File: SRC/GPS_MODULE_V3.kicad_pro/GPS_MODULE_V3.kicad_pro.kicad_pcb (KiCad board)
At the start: 4 copper layers, 53.7 x 41 mm, 141 parts, among them J1 Input, J2 Conn_02x02_Odd_Even, J3 nano_sim, J5 Conn_02x03_Odd_Even, Q1 SSM3J328R-HXY, Q2 BSN20, Q3 BSN20, Q5 2N7002, Q6 2N7002, Q7 2N7002, Q8 2N7002, Q9 2N7002, U1 ADP2504ACPZ-R7_3.3V_VERSION, U2 STM32F103C8Tx, U3 SIM7000E, U4 MAX485E, U7 ATA6561-GAQW-N, U8 W25Q32JVSS, Y1 8MHz, Y2 32.678KHz

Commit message: added logo
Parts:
- added G***: LOGO, MACHADA_footprints:ECOBODDA_medium, F.Cu at (247.8, 69.3)
- added G***: LOGO, MACHADA_footprints:GEVITON_LOGO_small, B.Cu at (271.5, 76.8)
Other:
- board text added: "001211223"
- board text added: "MADE IN KENYA"

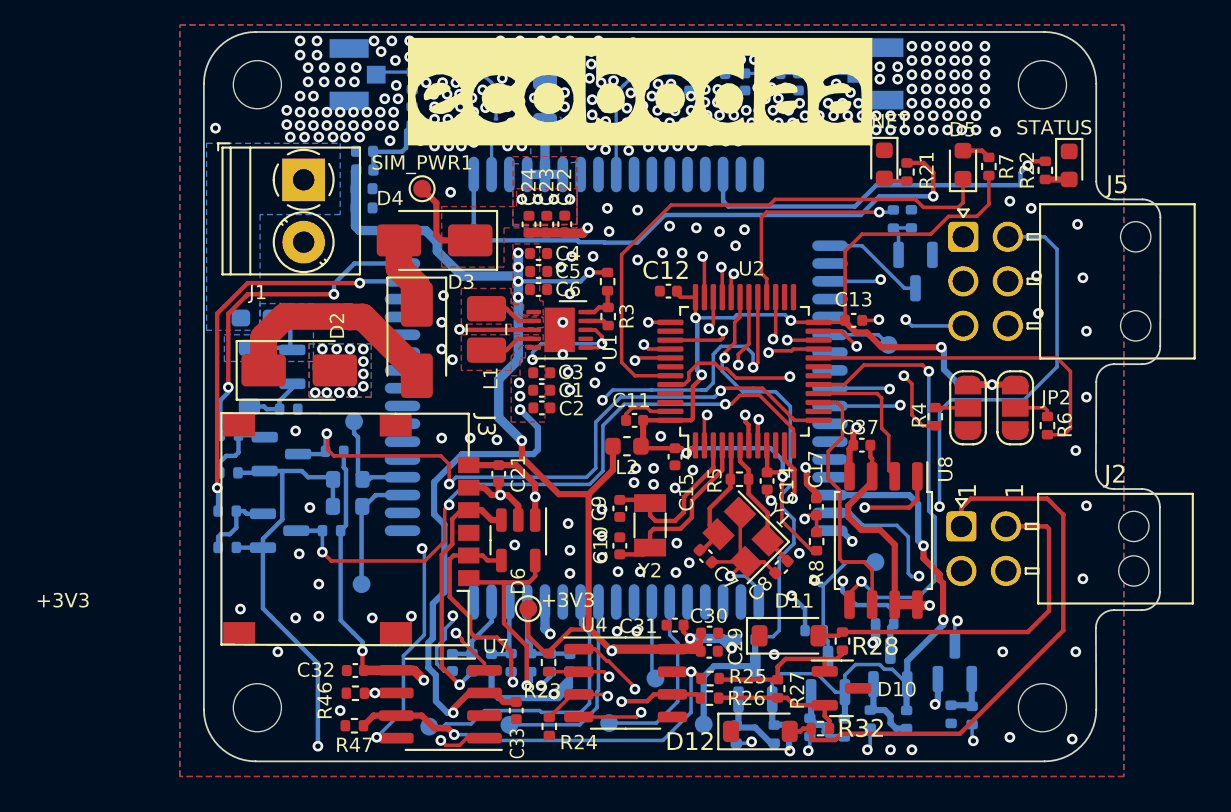
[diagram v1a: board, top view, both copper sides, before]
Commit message: gps update on buck 3v3
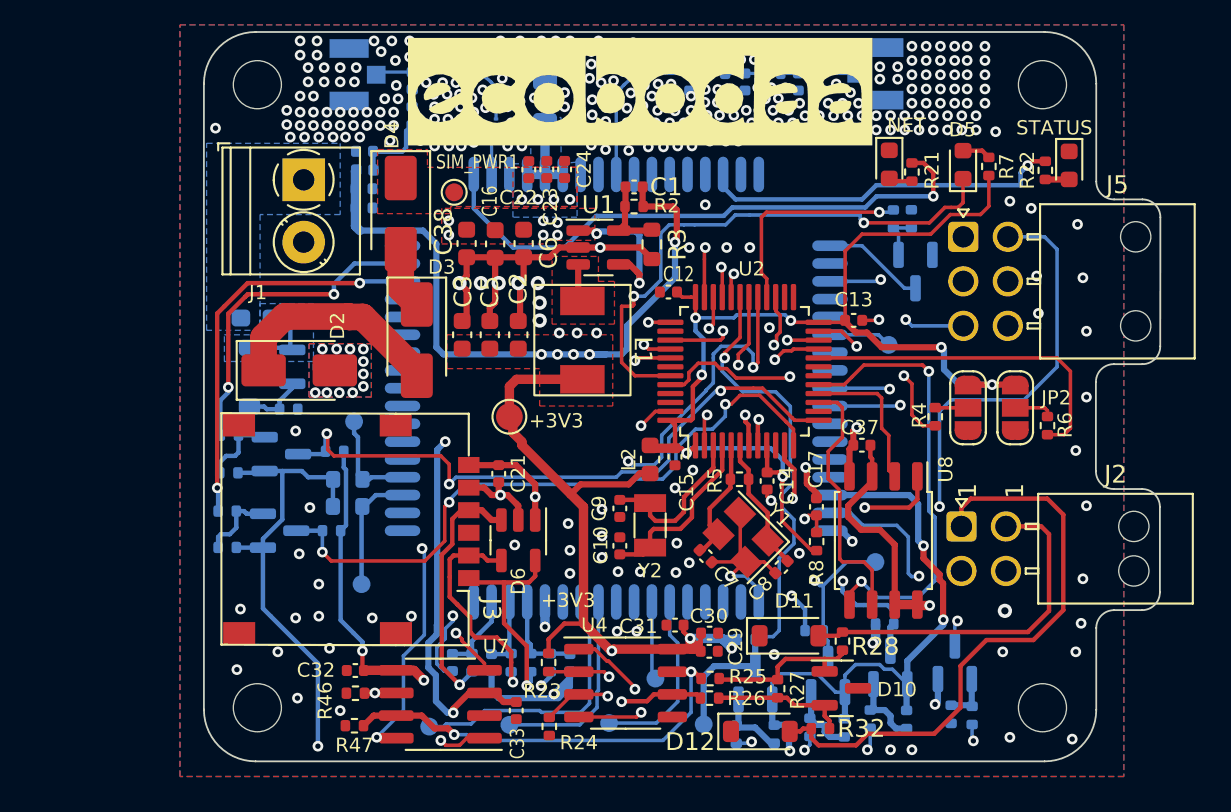
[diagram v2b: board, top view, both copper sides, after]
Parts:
- removed C11: 100n, Capacitor_SMD:C_0402_1005Metric
- removed C4: 10u, Capacitor_SMD:C_0402_1005Metric
- added C16: 10u, Capacitor_SMD:C_0603_1608Metric, F.Cu at (239.7, 77.9)
- added C38: 100n, Capacitor_SMD:C_0603_1608Metric, F.Cu at (238.1, 77.9)
- C1: value 10u -> 8.2p
- C2: value 100n -> 10n; footprint Capacitor_SMD:C_0402_1005Metric -> Capacitor_SMD:C_0603_1608Metric
- C3: value 10u -> 33p; footprint Capacitor_SMD:C_0402_1005Metric -> Capacitor_SMD:C_0603_1608Metric
- C5: value 100n -> 22u; footprint Capacitor_SMD:C_0402_1005Metric -> Capacitor_SMD:C_0603_1608Metric
- C6: footprint Capacitor_SMD:C_0402_1005Metric -> Capacitor_SMD:C_0603_1608Metric
- L1: value 1.5uH -> 2.2u; footprint Inductor_SMD:L_1008_2520Metric_Pad1.43x2.20mm_HandSolder -> greencharge-footprints:MDA5030-100M
- R2: value 1K -> 180K
- R3: value 1K -> 40K; footprint Resistor_SMD:R_0402_1005Metric -> Resistor_SMD:R_0603_1608Metric
- TP2: footprint TestPoint:TestPoint_Pad_D1.0mm -> TestPoint:TestPoint_Pad_D1.5mm
- U1: value ADP2504ACPZ-R7_3.3V_VERSION -> SY8089AAAC; footprint Package_DFN_QFN:DFN-10-1EP_3x3mm_P0.5mm_EP1.7x2.5mm -> Package_TO_SOT_SMD:SOT-23-5
- moved C1 12.5 mm to (247.5, 74.7), turned to 180 degrees
- moved TP2 10.8 mm to (240.5, 87.6)
- moved L1 5.62 mm to (244.6, 81.1), turned to -90 degrees
- moved U1 5.11 mm to (245.5, 78.1)
- moved C3 4.95 mm to (237.8, 83.0), turned to 90 degrees
- moved R3 4.74 mm to (248.5, 77.9)
- moved C5 4.49 mm to (239.4, 83.0), turned to 90 degrees
- moved R2 4.47 mm to (247.5, 75.8), turned to 180 degrees
- moved C2 4.31 mm to (241.0, 83.0), turned to 90 degrees
- moved C24 3.67 mm to (243.6, 73.7), turned to 90 degrees
- moved C22 3.67 mm to (241.6, 73.7), turned to 90 degrees
- moved C23 3.08 mm to (242.6, 73.7), turned to 90 degrees
- moved C6 2.71 mm to (241.3, 77.9), turned to -90 degrees
- moved D4 2.42 mm to (234.4, 76.2), turned to -90 degrees
- moved SIM_PWR1 1.81 mm to (237.4, 75.0)
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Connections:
- C1 pad 1: +5V -> +3V3
- C1 pad 2: GND -> Net-(U1-FB)
- C2 pad 1: +5V -> +3V3
- C3 pad 1: +5V -> +3V3
- C6 pad 1: +3V3 -> +5V
- L1 pad 1: Net-(U1-SW1) -> Net-(U1-LX)
- L1 pad 2: Net-(U1-SW2) -> +3V3
- U1 pad 1: +3V3 -> +5V
- U1 pad 2: Net-(U1-SW2) -> GND
- U1 pad 3: GND -> Net-(U1-LX)
- U1 pad 4: Net-(U1-SW1) -> +5V
- U1 pad 5: +5V -> Net-(U1-FB)
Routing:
- net GND: track 56.2 -> 69.3 mm, vias 396 -> 382
- net +3V3: track 131.5 -> 142.6 mm, vias 14 -> 13
- net 4.2V_SIMPWR: track 9.71 -> 4.75 mm
- net Net-(U1-SW2): track 2.93 -> 0.00 mm
- net Net-(U1-SW1): track 2.91 -> 0.00 mm
- net Net-(U1-FB): track 2.32 -> 4.49 mm
- net Net-(U1-LX): track 0.00 -> 2.15 mm
- net /STM32F103C8T6_MCU/3v3_stm: track 67.1 -> 65.2 mm
- net +5V: track 76.2 -> 78.1 mm, vias 17 -> 21
- net /CAN_TRANSCEIVER_ATA6561/CAN_RX: track 37.4 -> 38.8 mm
- net /CAN_TRANSCEIVER_ATA6561/CAN_TX: track 46.2 -> 47.4 mm
- net /RS485_MAX485/A: track 32.5 -> 33.3 mm
- net /SIM7000E_GPRS_SIM MODULE/STATUS: track 21.2 -> 20.4 mm
- net /STM32F103C8T6_MCU/RX2: track 37.1 -> 36.3 mm
- net /SIM7000E_GPRS_SIM MODULE/V_Sim: track 20.3 -> 19.5 mm
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- added copper zone on F.Cu, net Net-(U1-LX)
- removed copper zone on F.Cu, net Net-(U1-SW1)
- removed copper zone on F.Cu, net Net-(U1-SW2)

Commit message: updates on BOM, CPL and gerbers
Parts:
- removed BOOT_CFG1: BOOT_CFG, TestPoint:TestPoint_Pad_D1.0mm
- removed C35: 10n, Capacitor_SMD:C_0402_1005Metric
- removed C36: 1n, Capacitor_SMD:C_0402_1005Metric
- removed FL1: B39162B8813P810, Filter:Filter_1109-5_1.1x0.9mm
- removed the G*** at (247.8, 69.3)
- removed J5: Conn_02x03_Odd_Even, Connector_Molex:Molex_Nano-Fit_105314-xx06_2x03_P2.50mm_Horizontal
- removed L4: 27nH, Inductor_SMD:L_0402_1005Metric
- removed L5: 100mHz 150/200R, Inductor_SMD:L_0402_1005Metric
- removed MDM_LOG_TX1: MDM_LOG_TX, TestPoint:TestPoint_Pad_D1.0mm
- removed Q8, Q9: 2N7002, Package_TO_SOT_SMD:SOT-23
- removed SIM_RX1: Sim_RX, TestPoint:TestPoint_Pad_D1.0mm
- removed SIM_TX1: Sim_TX, TestPoint:TestPoint_Pad_D1.0mm
- added C11: 10u, Capacitor_SMD:C_0402_1005Metric, F.Cu at (245.5, 87.9)
- added C4: 1u, Capacitor_SMD:C_0402_1005Metric, F.Cu at (241.6, 87.8)
- added G***: LOGO, MACHADA_footprints:ECOBODDA_SMALL, B.Cu at (230.8, 97.7)
- added HST_RXD1: HST_RXD, brilliant-kicad-library:TestPoint_Pad_D0.9mm, F.Cu at (242.3, 68.0)
- added HST_TXD1: HST_TXD, brilliant-kicad-library:TestPoint_Pad_D0.9mm, F.Cu at (252.1, 67.3)
- added J4: Micro_SD_Card, MACHADA_footprints:MOLEX_503398-1892, B.Cu at (242.2, 99.2)
- added Q4: 2N7002, Package_TO_SOT_SMD:SOT-23, F.Cu at (254.4, 76.3)
- added R36: 1K, Resistor_SMD:R_0402_1005Metric, B.Cu at (260.7, 104.2)
- added R48: 10K, Resistor_SMD:R_0402_1005Metric, B.Cu at (254.4, 98.5)
- added R49: 10K, Resistor_SMD:R_0402_1005Metric, B.Cu at (256.1, 95.1)
- added R50: 1K, Resistor_SMD:R_0402_1005Metric, B.Cu at (251.6, 97.0)
- added U5: XC6206PxxxMR, Package_TO_SOT_SMD:SOT-23-3, F.Cu at (233.8, 70.1)
- C18: value 22p -> 10u; moved to F.Cu
- C19: value 22p -> 100u; footprint Capacitor_SMD:C_0402_1005Metric -> Capacitor_Tantalum_SMD:CP_EIA-3216-18_Kemet-A; moved to F.Cu
- C20: value 22p -> 1u
- C21: value 100n -> 22p; moved to B.Cu
- C22: value 1u -> 22p; moved to B.Cu
- C23: value 10u -> 22p; moved to B.Cu
- C24: value 10u -> 0.1u
- C25: value 100u -> 1u; footprint Capacitor_Tantalum_SMD:CP_EIA-3216-18_Kemet-A -> Capacitor_SMD:C_0402_1005Metric; moved to F.Cu
- C26: value 0.3p -> 0.1u; moved to F.Cu
- C27: value ~ -> 1u; moved to F.Cu
- C28: value ~ -> 0.1u
- C30, C31, JP1, JP2, R22, R4, R6: moved to B.Cu
- D+1, D-1, SIM_I2C_SCL1, SIM_I2C_SDA1: footprint TestPoint:TestPoint_Pad_D1.0mm -> brilliant-kicad-library:TestPoint_Pad_D0.9mm
- D6: value SP0504BAHT -> LXES15AAA1-153; footprint Package_TO_SOT_SMD:SOT-23-5 -> Diode_SMD:D_0402_1005Metric; moved to B.Cu
- D7: value ORANGE -> SP0504BAHT; footprint LED_SMD:LED_0603_1608Metric -> Package_TO_SOT_SMD:SOT-23-5; moved to B.Cu
- D8: value BLUE -> ORANGE; moved to B.Cu
- D9: value LXES15AAA1-153 -> BLUE; footprint Diode_SMD:D_0402_1005Metric -> LED_SMD:LED_0603_1608Metric
- J2: value Conn_02x02_Odd_Even -> Conn_02x04_Odd_Even; footprint Connector_Molex:Molex_Nano-Fit_105314-xx04_2x02_P2.50mm_Horizontal -> Connector_Molex:Molex_Mini-Fit_Jr_5569-08A2_2x04_P4.20mm_Horizontal
- L3: value 1uH -> 82nH
- Q3, Q6, R43, R44: moved to F.Cu
- R10: value 1k -> 10K
- R12: value 10K -> 1k
- R13: value 22R -> 1k; moved to F.Cu
- R14: value 22R -> 10K; moved to F.Cu
- R15: value 22R -> 2.2K
- R16: value 10K -> 2.2K
- R17, R18: value 2.2K -> 22R; footprint Resistor_SMD:R_0603_1608Metric -> Resistor_SMD:R_0402_1005Metric
- R19: value 0R -> 22R
- R20: value 10R -> 200K; moved to F.Cu
- R21: value 390R -> 100K
- R29: value 1K -> 390R
- R30, R31: value 1K -> 10K; moved to F.Cu
- R33, R45: value 10K -> 1K; moved to F.Cu
- R37, R38, R39, R42: value 10K -> 10k
- R40, R41: value 1K -> 10k
- U3: value SIM7000E -> A9G_MODULE; footprint Lib:SIMCON_SIM7000E -> MACHADA_footprints:A9G_MODULE
- USB_VBUS1: footprint TestPoint:TestPoint_Pad_D1.0mm -> brilliant-kicad-library:TestPoint_Pad_D0.9mm; moved to F.Cu
- moved R10 42.4 mm to (231.8, 80.1), turned to 0 degrees
- moved D8 41.4 mm to (230.8, 68.8)
- moved R29 40.6 mm to (235.0, 71.1), turned to 180 degrees
- moved D-1 40.1 mm to (250.1, 67.4), turned to 90 degrees
- moved AE2 39.1 mm to (268.8, 80.2), turned to 0 degrees
- moved R22 38.7 mm to (232.2, 69.1)
- moved SIM_I2C_SDA1 38.2 mm to (269.9, 91.0)
- moved D+1 38.1 mm to (247.1, 67.4), turned to 90 degrees
- moved C20 35.6 mm to (259.8, 73.8)
- moved R17 34.7 mm to (260.9, 72.8), turned to -90 degrees
- moved C37 34.3 mm to (229.9, 105.1), turned to -90 degrees
- moved R44 34.2 mm to (253.0, 68.3), turned to 0 degrees
- moved Q6 32.6 mm to (252.1, 70.6), turned to 0 degrees
- moved R43 32.3 mm to (249.6, 70.0), turned to -90 degrees
- moved R33 31.4 mm to (254.7, 74.0), turned to 0 degrees
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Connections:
- C18 pad 1: /SIM7000E_GPRS_SIM MODULE/Sim_DIO -> 4.2V_SIMPWR
- C19 pad 1: /SIM7000E_GPRS_SIM MODULE/Sim_CLK -> 4.2V_SIMPWR
- C20 pad 1: /SIM7000E_GPRS_SIM MODULE/Sim_RST -> /A9G_GSM_GPRS_MODULE/VIO
- C21 pad 1: /SIM7000E_GPRS_SIM MODULE/V_Sim -> /A9G_GSM_GPRS_MODULE/Sim_DIO
- C22 pad 1: 4.2V_SIMPWR -> /A9G_GSM_GPRS_MODULE/Sim_CLK
- C23 pad 1: 4.2V_SIMPWR -> /A9G_GSM_GPRS_MODULE/Sim_RST
- C26 pad 1: GND -> 2V8
- C26 pad 2: /SIM7000E_GPRS_SIM MODULE/RF_ANT -> GND
- C27 pad 1: GND -> 2V8
- C27 pad 2: Net-(C27-Pad2) -> GND
- C28 pad 1: GND -> /A9G_GSM_GPRS_MODULE/TF_CARD_CONN/2V8
- C28 pad 2: Net-(AE1-A) -> GND
- C34 pad 1: +3V3 -> /A9G_GSM_GPRS_MODULE/TF_CARD_CONN/2V8
- D+1 pad 1: Net-(U3-USB_DP) -> Net-(U3-USB_P)
- D-1 pad 1: Net-(U3-USB_DM) -> Net-(U3-USB_N)
- D6 pad 1: /SIM7000E_GPRS_SIM MODULE/V_Sim -> GND
- D6 pad 2: GND -> Net-(AE1-A)
- D7 pad 1: GND -> /A9G_GSM_GPRS_MODULE/V_Sim
- D7 pad 2: Net-(D7-A) -> GND
- D9 pad 2: Net-(AE1-A) -> Net-(D9-A)
- J2 pad 1: /RS485_MAX485/A -> GND
- J2 pad 3: /RS485_MAX485/B -> /RS485_MAX485/A
- J2 pad 4: GND -> /STM32F103C8T6_MCU/SW0
- J3 pad C1: /SIM7000E_GPRS_SIM MODULE/V_Sim -> /A9G_GSM_GPRS_MODULE/V_Sim
- L3 pad 1: /SIM7000E_GPRS_SIM MODULE/RF_ANT -> GND
- L3 pad 2: Net-(C27-Pad2) -> Net-(AE1-A)
- Q5 pad 1: /SIM7000E_GPRS_SIM MODULE/VDD_EXT -> 2V8
- Q5 pad 3: /STM32F103C8T6_MCU/TX1 -> /STM32F103C8T6_MCU/RX2
- Q6 pad 1: /SIM7000E_GPRS_SIM MODULE/VDD_EXT -> 2V8
- Q6 pad 3: /SIM7000E_GPRS_SIM MODULE/SIM_DTR -> /STM32F103C8T6_MCU/TX2
- Q7 pad 1: /SIM7000E_GPRS_SIM MODULE/VDD_EXT -> 2V8
- Q7 pad 3: /STM32F103C8T6_MCU/RX1 -> /STM32F103C8T6_MCU/TX1
- R10 pad 1: /SIM7000E_GPRS_SIM MODULE/Sim_Reset -> GND
- R10 pad 2: Net-(Q3-G) -> Net-(Q2-G)
- R11 pad 1: GND -> Net-(Q3-D)
- R11 pad 2: Net-(Q2-G) -> /A9G_GSM_GPRS_MODULE/VIO
- R12 pad 1: GND -> /A9G_GSM_GPRS_MODULE/IO29
- R12 pad 2: Net-(Q3-G) -> Net-(Q3-D)
- R13 pad 1: /SIM7000E_GPRS_SIM MODULE/Sim_RST -> /A9G_GSM_GPRS_MODULE/PWRKEY
- R13 pad 2: Net-(J3-RST) -> Net-(Q3-G)
- R14 pad 1: /SIM7000E_GPRS_SIM MODULE/Sim_CLK -> GND
- R14 pad 2: Net-(J3-CLK) -> Net-(Q3-G)
- R15 pad 1: /SIM7000E_GPRS_SIM MODULE/Sim_DIO -> Net-(U3-I2C2_SCL/IO19)
- R15 pad 2: Net-(J3-I/O) -> /A9G_GSM_GPRS_MODULE/VIO
- R16 pad 1: /SIM7000E_GPRS_SIM MODULE/Sim_DIO -> Net-(U3-I2C2_SDA/IO20)
- R16 pad 2: /SIM7000E_GPRS_SIM MODULE/V_Sim -> /A9G_GSM_GPRS_MODULE/VIO
- R17 pad 1: Net-(U3-I2C_SCL) -> /A9G_GSM_GPRS_MODULE/Sim_RST
- R17 pad 2: /SIM7000E_GPRS_SIM MODULE/VDD_EXT -> Net-(J3-RST)
- R18 pad 1: Net-(U3-I2C_SDA) -> /A9G_GSM_GPRS_MODULE/Sim_CLK
- R18 pad 2: /SIM7000E_GPRS_SIM MODULE/VDD_EXT -> Net-(J3-CLK)
- R19 pad 1: Net-(C27-Pad2) -> /A9G_GSM_GPRS_MODULE/Sim_DIO
- R19 pad 2: Net-(AE1-A) -> Net-(J3-I/O)
- R20 pad 1: Net-(L4-Pad1) -> Net-(U3-ADC0)
- R20 pad 2: /SIM7000E_GPRS_SIM MODULE/gps_VDD -> 4.2V_SIMPWR
- R21 pad 1: /SIM7000E_GPRS_SIM MODULE/NETLIGHT -> GND
- R21 pad 2: Net-(D7-A) -> Net-(U3-ADC0)
- R22 pad 1: /SIM7000E_GPRS_SIM MODULE/STATUS -> /A9G_GSM_GPRS_MODULE/GPRS_NET-STATUS
- R29 pad 1: /SIM7000E_GPRS_SIM MODULE/MOSFET_LOGIC_LEVEL_TRANSLATOR/LOW_SIDE_SIM_RXD_LOGIC -> /A9G_GSM_GPRS_MODULE/GPS POSITION
- R29 pad 2: Net-(Q5-S) -> Net-(D9-A)
- R30 pad 1: /SIM7000E_GPRS_SIM MODULE/MOSFET_LOGIC_LEVEL_TRANSLATOR/LOW_SIDE_SIM_DTR_LOGIC -> 2V8
- R30 pad 2: Net-(Q6-S) -> Net-(Q4-S)
- R31 pad 1: /SIM7000E_GPRS_SIM MODULE/MOSFET_LOGIC_LEVEL_TRANSLATOR/LOW_SIDE_SIM_TXD_LOGIC -> +3V3
- R31 pad 2: Net-(Q7-S) -> /STM32F103C8T6_MCU/RX1
- R33 pad 1: /SIM7000E_GPRS_SIM MODULE/VDD_EXT -> /A9G_GSM_GPRS_MODULE/MOSFET_LOGIC_LEVEL_TRANSLATOR9/LOW_SIDE_LOGIC_SIGNAL
- R33 pad 2: Net-(Q5-S) -> Net-(Q4-S)
- R34 pad 1: /SIM7000E_GPRS_SIM MODULE/VDD_EXT -> 2V8
- R34 pad 2: Net-(Q6-S) -> Net-(Q5-S)
- R35 pad 1: /SIM7000E_GPRS_SIM MODULE/VDD_EXT -> +3V3
- R35 pad 2: Net-(Q7-S) -> /STM32F103C8T6_MCU/RX2
- R37 pad 1: +3V3 -> /A9G_GSM_GPRS_MODULE/TF_CARD_CONN/2V8
- R37 pad 2: /STM32F103C8T6_MCU/TX1 -> /A9G_GSM_GPRS_MODULE/TF_CARD_CONN/SD_D2
- R38 pad 1: +3V3 -> /A9G_GSM_GPRS_MODULE/TF_CARD_CONN/2V8
- R38 pad 2: /SIM7000E_GPRS_SIM MODULE/SIM_DTR -> /A9G_GSM_GPRS_MODULE/TF_CARD_CONN/SD_D3
- R39 pad 1: +3V3 -> /A9G_GSM_GPRS_MODULE/TF_CARD_CONN/2V8
- R39 pad 2: /STM32F103C8T6_MCU/RX1 -> /A9G_GSM_GPRS_MODULE/TF_CARD_CONN/SD_CMD
- R40 pad 1: /SIM7000E_GPRS_SIM MODULE/GPS_RXD_ -> /A9G_GSM_GPRS_MODULE/TF_CARD_CONN/2V8
- R40 pad 2: Net-(Q8-S) -> /A9G_GSM_GPRS_MODULE/TF_CARD_CONN/SD_D0
- R41 pad 1: /SIM7000E_GPRS_SIM MODULE/GPS_TXD_ -> /A9G_GSM_GPRS_MODULE/TF_CARD_CONN/2V8
- R41 pad 2: Net-(Q9-S) -> /A9G_GSM_GPRS_MODULE/TF_CARD_CONN/SD_D1
- R42 pad 1: /SIM7000E_GPRS_SIM MODULE/VDD_EXT -> /A9G_GSM_GPRS_MODULE/TF_CARD_CONN/2V8
- R42 pad 2: Net-(Q8-S) -> /A9G_GSM_GPRS_MODULE/TF_CARD_CONN/SD_CLK
- R43 pad 1: /SIM7000E_GPRS_SIM MODULE/VDD_EXT -> 2V8
- R43 pad 2: Net-(Q9-S) -> Net-(Q6-S)
- R45 pad 1: +3V3 -> /A9G_GSM_GPRS_MODULE/MOSFET_LOGIC_LEVEL_TRANSLATOR7/LOW_SIDE_LOGIC_SIGNAL
- R45 pad 2: /STM32F103C8T6_MCU/RX2 -> Net-(Q6-S)
- R9 pad 1: /SIM7000E_GPRS_SIM MODULE/PWRKEY -> /A9G_GSM_GPRS_MODULE/Sim_Restart
- SIM_I2C_SCL1 pad 1: Net-(U3-I2C_SCL) -> Net-(U3-I2C2_SCL/IO19)
- SIM_I2C_SDA1 pad 1: Net-(U3-I2C_SDA) -> Net-(U3-I2C2_SDA/IO20)
- U2 pad 28: /SIM7000E_GPRS_SIM MODULE/PWRKEY -> /A9G_GSM_GPRS_MODULE/PWRKEY
- U2 pad 40: /SIM7000E_GPRS_SIM MODULE/Sim_Reset -> /A9G_GSM_GPRS_MODULE/Sim_Restart
- U2 pad 41: /SIM7000E_GPRS_SIM MODULE/SIM_DTR -> /STM32F103C8T6_MCU/Sim_DTR
- U3 pad 1: Net-(Q2-D) -> Net-(U3-I2C2_SCL/IO19)
- U3 pad 10: /SIM7000E_GPRS_SIM MODULE/MOSFET_LOGIC_LEVEL_TRANSLATOR/LOW_SIDE_SIM_RXD_LOGIC -> GND
- U3 pad 11: unconnected-(U3-PCM_CLK-Pad11) -> 4.2V_SIMPWR
- U3 pad 12: unconnected-(U3-PCM_SYNC-Pad12) -> 4.2V_SIMPWR
- U3 pad 15: /SIM7000E_GPRS_SIM MODULE/VDD_EXT -> Net-(U3-ADC0)
- U3 pad 16: Net-(Q3-D) -> unconnected-(U3-ADC1-Pad16)
- U3 pad 17: GND -> Net-(U3-VUSB_DET)
- U3 pad 18: GND -> Net-(Q2-D)
- U3 pad 19: (no net) -> unconnected-(U3-LCD_CS/I2S_LRCK/IO15-Pad19)
- U3 pad 2: GND -> Net-(U3-I2C2_SDA/IO20)
- U3 pad 20: (no net) -> unconnected-(U3-LCD_RSTB/I2S_BCK/IO14-Pad20)
- U3 pad 21: (no net) -> unconnected-(U3-LCD_DIO/I2S_DO/IO17-Pad21)
- U3 pad 22: (no net) -> unconnected-(U3-LCD_DC/IO18-Pad22)
- U3 pad 23: Net-(U3-MDM_LOG_TX) -> unconnected-(U3-LCD_SCK/I2S_DI/IO16-Pad23)
- U3 pad 24: Net-(U3-USB_VBUS) -> /A9G_GSM_GPRS_MODULE/IO29
- U3 pad 26: (no net) -> /A9G_GSM_GPRS_MODULE/GPRS_NET-STATUS
- U3 pad 27: Net-(U3-USB_DP) -> GND
- U3 pad 28: Net-(U3-USB_DM) -> /A9G_GSM_GPRS_MODULE/Sim_CLK
- U3 pad 29: GND -> /A9G_GSM_GPRS_MODULE/V_Sim
- U3 pad 3: /SIM7000E_GPRS_SIM MODULE/MOSFET_LOGIC_LEVEL_TRANSLATOR/LOW_SIDE_SIM_DTR_LOGIC -> /A9G_GSM_GPRS_MODULE/TF_CARD_CONN/SD_D3
- U3 pad 30: /SIM7000E_GPRS_SIM MODULE/V_Sim -> /A9G_GSM_GPRS_MODULE/Sim_DIO
- U3 pad 31: /SIM7000E_GPRS_SIM MODULE/Sim_DIO -> Net-(U3-HST_RXD)
- U3 pad 32: /SIM7000E_GPRS_SIM MODULE/Sim_CLK -> Net-(U3-HST_TXD)
- U3 pad 33: /SIM7000E_GPRS_SIM MODULE/Sim_RST -> Net-(U3-USB_P)
- U3 pad 34: /SIM7000E_GPRS_SIM MODULE/Sim_DET -> Net-(U3-USB_N)
- U3 pad 35: (no net) -> unconnected-(U3-MIC_P-Pad35)
- U3 pad 36: (no net) -> unconnected-(U3-MIC_N-Pad36)
- U3 pad 37: Net-(U3-I2C_SDA) -> unconnected-(U3-IO25-Pad37)
- U3 pad 38: Net-(U3-I2C_SCL) -> unconnected-(U3-IO30-Pad38)
- U3 pad 39: GND -> /A9G_GSM_GPRS_MODULE/GPS POSITION
- U3 pad 4: unconnected-(U3-RI-Pad4) -> /A9G_GSM_GPRS_MODULE/TF_CARD_CONN/SD_D2
- U3 pad 40: (no net) -> GND
- U3 pad 41: (no net) -> Net-(AE1-A)
- U3 pad 42: (no net) -> /A9G_GSM_GPRS_MODULE/Sim_RST
- U3 pad 43: (no net) -> /A9G_GSM_GPRS_MODULE/VIO
- U3 pad 44: (no net) -> GND
- U3 pad 45: GND -> Net-(AE2-A)
- U3 pad 46: GND -> unconnected-(U3-GND-Pad46)
- U3 pad 47: (no net) -> unconnected-(U3-UART2_RTS/I2C3_SDA/IO7-Pad47)
- U3 pad 49: /SIM7000E_GPRS_SIM MODULE/GPS_RXD_ -> /A9G_GSM_GPRS_MODULE/MOSFET_LOGIC_LEVEL_TRANSLATOR7/LOW_SIDE_LOGIC_SIGNAL
- U3 pad 5: unconnected-(U3-DCD-Pad5) -> /A9G_GSM_GPRS_MODULE/TF_CARD_CONN/SD_D1
- U3 pad 50: /SIM7000E_GPRS_SIM MODULE/GPS_TXD_ -> /A9G_GSM_GPRS_MODULE/MOSFET_LOGIC_LEVEL_TRANSLATOR6/LOW_SIDE_LOGIC_SIGNAL
- U3 pad 51: (no net) -> unconnected-(U3-UART1_RTS/IO3-Pad51)
- U3 pad 52: /SIM7000E_GPRS_SIM MODULE/NETLIGHT -> unconnected-(U3-UART1_CTS/IO2-Pad52)
- U3 pad 53: /SIM7000E_GPRS_SIM MODULE/GNSS_ANT -> /A9G_GSM_GPRS_MODULE/MOSFET_LOGIC_LEVEL_TRANSLATOR8/LOW_SIDE_LOGIC_SIGNAL
- U3 pad 54: GND -> /A9G_GSM_GPRS_MODULE/MOSFET_LOGIC_LEVEL_TRANSLATOR9/LOW_SIDE_LOGIC_SIGNAL
- U3 pad 55: 4.2V_SIMPWR -> GND
- U3 pad 56: 4.2V_SIMPWR -> GND
- U3 pad 6: Net-(U3-BOOT_CFG) -> /A9G_GSM_GPRS_MODULE/TF_CARD_CONN/SD_D0
- U3 pad 7: unconnected-(U3-CTS-Pad7) -> /A9G_GSM_GPRS_MODULE/TF_CARD_CONN/SD_CMD
- U3 pad 8: unconnected-(U3-RTS-Pad8) -> /A9G_GSM_GPRS_MODULE/TF_CARD_CONN/SD_CLK
- U3 pad 9: /SIM7000E_GPRS_SIM MODULE/MOSFET_LOGIC_LEVEL_TRANSLATOR/LOW_SIDE_SIM_TXD_LOGIC -> Net-(Q3-D)
- USB_VBUS1 pad 1: Net-(U3-USB_VBUS) -> Net-(U3-VUSB_DET)
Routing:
- net +3V3: track 142.6 -> 0.00 mm, vias 13 -> 0
- net /SIM7000E_GPRS_SIM MODULE/VDD_EXT: track 86.8 -> 0.00 mm, vias 4 -> 0
- net +5V: track 78.1 -> 0.00 mm, vias 21 -> 0
- net GND: track 69.3 -> 0.00 mm, vias 382 -> 0
- net /STM32F103C8T6_MCU/3v3_stm: track 65.2 -> 0.00 mm, vias 7 -> 0
- net /CAN_TRANSCEIVER_ATA6561/CAN_TX: track 47.4 -> 0.00 mm, vias 2 -> 0
- net /CAN_TRANSCEIVER_ATA6561/CAN_STBY: track 45.2 -> 0.00 mm, vias 4 -> 0
- net /STM32F103C8T6_MCU/mcu_reset: track 43.8 -> 0.00 mm, vias 3 -> 0
- net /SIM7000E_GPRS_SIM MODULE/Sim_Reset: track 43.4 -> 0.00 mm, vias 3 -> 0
- net /STM32F103C8T6_MCU/TX3: track 43.3 -> 0.00 mm, vias 2 -> 0
- net /STM32F103C8T6_MCU/RX3: track 43.2 -> 0.00 mm, vias 2 -> 0
- net /RS485_MAX485/RS485_DE: track 40.8 -> 0.00 mm, vias 2 -> 0
- net /CAN_TRANSCEIVER_ATA6561/CAN_RX: track 38.8 -> 0.00 mm, vias 2 -> 0
- net /RS485_MAX485/RS485_~{RE}: track 37.2 -> 0.00 mm, vias 2 -> 0
- net /STM32F103C8T6_MCU/TX2: track 37.0 -> 0.00 mm, vias 3 -> 0
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- removed copper zone on F.Cu, net +3V3
- removed copper zone on B.Cu, net 4.2V_SIMPWR
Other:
- outline, holes or cut-outs redrawn

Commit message: routing
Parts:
- removed C19: 100u, Capacitor_Tantalum_SMD:CP_EIA-3216-18_Kemet-A
- removed J2: Conn_02x04_Odd_Even, Connector_Molex:Molex_Mini-Fit_Jr_5569-08A2_2x04_P4.20mm_Horizontal
- added C36: 100u, Capacitor_Tantalum_SMD:CP_EIA-3216-18_Kemet-A, F.Cu at (245.7, 92.1)
- added C39: 100u, Capacitor_Tantalum_SMD:CP_EIA-3216-18_Kemet-A, F.Cu at (243.6, 92.1)
- added J5: Conn_02x06_Counter_Clockwise, MACHADA_footprints:auto_jae_conn_02x06_p2.5mm_MX23A12NF1, F.Cu at (279.6, 87.0)
- D10, H3, H4, R27: moved to B.Cu
- D8, D9, R22, R29: moved to F.Cu
- moved C27 36.1 mm to (266.0, 67.8), turned to -90 degrees
- moved C26 33.7 mm to (264.9, 67.8), turned to -90 degrees
- moved AE1 32.3 mm to (232.2, 69.7), turned to -90 degrees
- moved U5 28.4 mm to (262.2, 68.2), turned to 180 degrees
- moved C25 26.6 mm to (261.1, 71.6), turned to 0 degrees
- moved C24 26.4 mm to (261.1, 70.5), turned to 0 degrees
- moved D6 24.9 mm to (235.9, 69.3), turned to -90 degrees
- moved L3 22.7 mm to (237.0, 69.3)
- moved D8 18.7 mm to (249.5, 68.2)
- moved C22 17.4 mm to (257.7, 67.6)
- moved R18 17.4 mm to (256.5, 67.5)
- moved SIM_PWR1 17.2 mm to (244.2, 84.7), turned to 90 degrees
- moved R22 16.0 mm to (248.1, 68.5)
- moved R29 11.1 mm to (245.4, 67.3), turned to 90 degrees
- moved R46 9.69 mm to (229.8, 99.6), turned to 90 degrees
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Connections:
- C28 pad 1: /A9G_GSM_GPRS_MODULE/TF_CARD_CONN/2V8 -> 2V8
- C34 pad 1: /A9G_GSM_GPRS_MODULE/TF_CARD_CONN/2V8 -> 2V8
- HST_RXD1 pad 1: Net-(U3-HST_RXD) -> Net-(U3-HST_TXD)
- HST_TXD1 pad 1: Net-(U3-HST_TXD) -> Net-(U3-HST_RXD)
- J4 pad 4: /A9G_GSM_GPRS_MODULE/TF_CARD_CONN/2V8 -> 2V8
- R37 pad 1: /A9G_GSM_GPRS_MODULE/TF_CARD_CONN/2V8 -> 2V8
- R38 pad 1: /A9G_GSM_GPRS_MODULE/TF_CARD_CONN/2V8 -> 2V8
- R39 pad 1: /A9G_GSM_GPRS_MODULE/TF_CARD_CONN/2V8 -> 2V8
- R40 pad 1: /A9G_GSM_GPRS_MODULE/TF_CARD_CONN/2V8 -> 2V8
- R41 pad 1: /A9G_GSM_GPRS_MODULE/TF_CARD_CONN/2V8 -> 2V8
- R42 pad 1: /A9G_GSM_GPRS_MODULE/TF_CARD_CONN/2V8 -> 2V8
- U3 pad 28: /A9G_GSM_GPRS_MODULE/Sim_CLK -> Net-(AE1-A)
- U3 pad 29: /A9G_GSM_GPRS_MODULE/V_Sim -> GND
- U3 pad 30: /A9G_GSM_GPRS_MODULE/Sim_DIO -> /A9G_GSM_GPRS_MODULE/GPS POSITION
- U3 pad 31: Net-(U3-HST_RXD) -> unconnected-(U3-IO30-Pad31)
- U3 pad 32: Net-(U3-HST_TXD) -> unconnected-(U3-IO25-Pad32)
- U3 pad 33: Net-(U3-USB_P) -> unconnected-(U3-MIC_N-Pad33)
- U3 pad 34: Net-(U3-USB_N) -> unconnected-(U3-MIC_P-Pad34)
- U3 pad 35: unconnected-(U3-MIC_P-Pad35) -> Net-(U3-USB_N)
- U3 pad 36: unconnected-(U3-MIC_N-Pad36) -> Net-(U3-USB_P)
- U3 pad 37: unconnected-(U3-IO25-Pad37) -> Net-(U3-HST_TXD)
- U3 pad 38: unconnected-(U3-IO30-Pad38) -> Net-(U3-HST_RXD)
- U3 pad 39: /A9G_GSM_GPRS_MODULE/GPS POSITION -> /A9G_GSM_GPRS_MODULE/Sim_DIO
- U3 pad 40: GND -> /A9G_GSM_GPRS_MODULE/V_Sim
- U3 pad 41: Net-(AE1-A) -> /A9G_GSM_GPRS_MODULE/Sim_CLK
- U3 pad 46: unconnected-(U3-GND-Pad46) -> GND
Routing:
- net +3V3: track 0.00 -> 48.5 mm, vias 0 -> 7
- net /A9G_GSM_GPRS_MODULE/V_Sim: track 0.00 -> 43.0 mm, vias 0 -> 3
- net /STM32F103C8T6_MCU/3v3_stm: track 0.00 -> 42.3 mm, vias 0 -> 4
- net Net-(J3-I/O): track 0.00 -> 41.7 mm, vias 0 -> 4
- net Net-(J3-RST): track 0.00 -> 41.5 mm, vias 0 -> 1
- net Net-(J3-CLK): track 0.00 -> 40.5 mm, vias 0 -> 4
- net GND: track 0.00 -> 31.9 mm, vias 0 -> 8
- net A_to_CANL: track 0.00 -> 27.4 mm, vias 0 -> 1
- net /A9G_GSM_GPRS_MODULE/TF_CARD_CONN/SD_CLK: track 0.00 -> 25.5 mm, vias 0 -> 2
- net /A9G_GSM_GPRS_MODULE/TF_CARD_CONN/SD_CMD: track 0.00 -> 25.4 mm, vias 0 -> 2
- net /A9G_GSM_GPRS_MODULE/TF_CARD_CONN/SD_D0: track 0.00 -> 24.0 mm, vias 0 -> 2
- net B_to_CANH: track 0.00 -> 23.4 mm, vias 0 -> 3
- net /CAN_TRANSCEIVER_ATA6561/CAN_RX: track 0.00 -> 22.4 mm, vias 0 -> 2
- net /A9G_GSM_GPRS_MODULE/TF_CARD_CONN/SD_D1: track 0.00 -> 21.9 mm, vias 0 -> 2
- net /A9G_GSM_GPRS_MODULE/TF_CARD_CONN/SD_D3: track 0.00 -> 18.0 mm, vias 0 -> 2
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- added copper zone on F.Cu, net +3V3
- added copper zone on B.Cu, net 4.2V_SIMPWR
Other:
- board text added: "SIM_P"

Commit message: completed GPS
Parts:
- removed SIM_I2C_SCL1: SIM_I2C_SCL, brilliant-kicad-library:TestPoint_Pad_D0.9mm
- removed SIM_I2C_SDA1: SIM_I2C_SDA, brilliant-kicad-library:TestPoint_Pad_D0.9mm
- moved J4 3.26 mm to (239.1, 100.0), turned to 0 degrees
- moved C20 2.36 mm to (262.2, 71.3), turned to 90 degrees
- moved C5 1.16 mm to (239.0, 78.6)
- moved C24 0.65 mm to (260.5, 70.5)
- moved C25 0.62 mm to (260.5, 71.6)
- moved G*** 0.51 mm to (230.3, 97.7)
- moved C8 0.15 mm to (255.8, 95.9)
- moved J1 0.11 mm to (228.9, 74.2)
- moved C32 0.10 mm to (236.4, 105.1)
- moved U8 0.09 mm to (243.8, 101.5)
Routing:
- net 2V8: track 12.5 -> 150.0 mm, vias 0 -> 8
- net +3V3: track 48.5 -> 129.9 mm, vias 7 -> 15
- net +5V: track 15.5 -> 90.6 mm
- net GND: track 31.9 -> 102.1 mm, vias 8 -> 253
- net /RS485_MAX485/RS485_DE: track 4.09 -> 51.9 mm, vias 1 -> 2
- net /A9G_GSM_GPRS_MODULE/MOSFET_LOGIC_LEVEL_TRANSLATOR6/LOW_SIDE_LOGIC_SIGNAL: track 0.00 -> 44.1 mm
- net /STM32F103C8T6_MCU/BOOT1: track 0.00 -> 37.3 mm, vias 0 -> 3
- net /A9G_GSM_GPRS_MODULE/IO29: track 6.77 -> 42.6 mm, vias 1 -> 2
- net /A9G_GSM_GPRS_MODULE/VIO: track 14.5 -> 47.2 mm, vias 0 -> 3
- net /STM32F103C8T6_MCU/TX1: track 1.32 -> 33.6 mm, vias 1 -> 2
- net 4.2V_SIMPWR: track 2.10 -> 33.9 mm, vias 5 -> 6
- net /FLASH_MEMORY/MISO: track 6.77 -> 37.8 mm
- net /FLASH_MEMORY/MOSI: track 3.12 -> 33.8 mm, vias 1 -> 4
- net /STM32F103C8T6_MCU/SW0: track 0.00 -> 29.6 mm, vias 0 -> 1
- net /RS485_MAX485/A: track 0.00 -> 28.4 mm
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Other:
- board size 53.7 x 41 mm -> 50.1 x 41 mm
- board text added: "netlight"
- board text added: "pwr in"
